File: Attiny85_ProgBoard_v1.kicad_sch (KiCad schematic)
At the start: 1 part, among them U1 ATtiny85V-10PU

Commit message: Designed PCB
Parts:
- added J1, J2, J3, J4, J5, J6, J7, J8: Conn_01x01_Female, Connector_Pin:PinHole_01x01, symbol Connector:Conn_01x01_Female
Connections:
- net at U1.1 (~{RESET}/PB5): now also J7.1 (Pin_1)
- net at U1.2 (XTAL1/PB3): now also J5.1 (Pin_1)
- net at U1.3 (XTAL2/PB4): now also J6.1 (Pin_1)
- net at U1.4 (GND): now also J8.1 (Pin_1)
- net at U1.5 (AREF/PB0): now also J2.1 (Pin_1)
- net at U1.6 (PB1): now also J3.1 (Pin_1)
- net at U1.7 (PB2): now also J4.1 (Pin_1)
- net at U1.8 (VCC): now also J1.1 (Pin_1)
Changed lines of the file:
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@@
 (kicad_sch (version 20230121) (generator eeschema)
   (paper "A4")
+  (wire (pts (xy 120.65 60.96) (xy 138.43 60.96))
+    (stroke (width 0) (type default))
+  )
+  (wire (pts (xy 135.89 71.12) (xy 151.13 71.12))
+    (stroke (width 0) (type default))
+  )
+  (wire (pts (xy 138.43 78.74) (xy 135.89 78.74))
+    (stroke (width 0) (type default))
+  )
+  (wire (pts (xy 135.89 88.9) (xy 152.4 88.9))
+    (stroke (width 0) (type default))
+  )
+  (wire (pts (xy 152.4 86.36) (xy 138.43 86.36))
+    (stroke (width 0) (type default))
+  )
+  (wire (pts (xy 135.89 76.2) (xy 140.97 76.2))
+    (stroke (width 0) (type default))
+  )
+  (wire (pts (xy 138.43 86.36) (xy 138.43 78.74))
+    (stroke (width 0) (type default))
+  )
+  (wire (pts (xy 135.89 73.66) (xy 151.13 73.66))
+    (stroke (width 0) (type default))
+  )
+  (wire (pts (xy 120.65 91.44) (xy 152.4 91.44))
+    (stroke (width 0) (type default))
+  )
+  (wire (pts (xy 140.97 83.82) (xy 152.4 83.82))
+    (stroke (width 0) (type default))
+  )
+  (wire (pts (xy 135.89 81.28) (xy 135.89 88.9))
+    (stroke (width 0) (type default))
+  )
+  (wire (pts (xy 138.43 66.04) (xy 138.43 60.96))
+    (stroke (width 0) (type default))
+  )
+  (wire (pts (xy 140.97 76.2) (xy 140.97 83.82))
+    (stroke (width 0) (type default))
+  )
+  (wire (pts (xy 151.13 66.04) (xy 138.43 66.04))
+    (stroke (width 0) (type default))
+  )
+  (wire (pts (xy 135.89 68.58) (xy 151.13 68.58))
+    (stroke (width 0) (type default))
+  )
   (symbol (lib_id "Attiny85_ProgBoard_v1-rescue:ATtiny85V-10PU-MCU_Microchip_ATtiny") (at 120.65 76.2 0) (unit 1)
     (in_bom yes) (on_board yes) (dnp no)
@@
         )
       )
+    )
+  )
+  (symbol (lib_id "Connector:Conn_01x01_Female") (at 157.48 88.9 0) (unit 1)
+    (in_bom yes) (on_board yes) (dnp no) (fields_autoplaced)
+    (property "Reference" "J7" (at 158.75 88.265 0)
+      (effects (font (size 1.27 1.27)) (justify left))
+    )
+    (property "Value" "Conn_01x01_Female" (at 158.75 90.805 0)
+      (effects (font (size 1.27 1.27)) (justify left))
+    )
+    (property "Footprint" "Connector_Pin:PinHole_01x01" (at 157.48 88.9 0)
+      (effects (font (size 1.27 1.27)) hide)
+    )
+    (property "Datasheet" "~" (at 157.48 88.9 0)
+      (effects (font (size 1.27 1.27)) hide)
+    )
+    (pin "1")
+    (instances
+      (project "Attiny85_ProgBoard_v1"
+        (path "/461172af-f3d0-444f-a1ea-3ea6bb3ec9d2"
+          (reference "J7") (unit 1)
+        )
+      )
+    )
+  )
+  (symbol (lib_id "Connector:Conn_01x01_Female") (at 156.21 73.66 0) (unit 1)
+    (in_bom yes) (on_board yes) (dnp no) (fields_autoplaced)
+    (property "Reference" "J4" (at 157.48 73.025 0)
+      (effects (font (size 1.27 1.27)) (justify left))
+    )
+    (property "Value" "Conn_01x01_Female" (at 157.48 75.565 0)
+      (effects (font (size 1.27 1.27)) (justify left))
+    )
+    (property "Footprint" "Connector_Pin:PinHole_01x01" (at 156.21 73.66 0)
+      (effects (font (size 1.27 1.27)) hide)
+    )
+    (property "Datasheet" "~" (at 156.21 73.66 0)
+      (effects (font (size 1.27 1.27)) hide)
+    )
+    (pin "1")
+    (instances
+      (project "Attiny85_ProgBoard_v1"
+        (path "/461172af-f3d0-444f-a1ea-3ea6bb3ec9d2"
+          (reference "J4") (unit 1)
+        )
+      )
+    )
+  )
+  (symbol (lib_id "Connector:Conn_01x01_Female") (at 156.21 66.04 0) (unit 1)
+    (in_bom yes) (on_board yes) (dnp no) (fields_autoplaced)
+    (property "Reference" "J1" (at 157.48 65.405 0)
+      (effects (font (size 1.27 1.27)) (justify left))
+    )
+    (property "Value" "Conn_01x01_Female" (at 157.48 67.945 0)
+      (effects (font (size 1.27 1.27)) (justify left))
+    )
+    (property "Footprint" "Connector_Pin:PinHole_01x01" (at 156.21 66.04 0)
+      (effects (font (size 1.27 1.27)) hide)
+    )
+    (property "Datasheet" "~" (at 156.21 66.04 0)
+      (effects (font (size 1.27 1.27)) hide)
+    )
+    (pin "1")
+    (instances
+      (project "Attiny85_ProgBoard_v1"
+        (path "/461172af-f3d0-444f-a1ea-3ea6bb3ec9d2"
+          (reference "J1") (unit 1)
+        )
+      )
+    )
+  )
+  (symbol (lib_id "Connector:Conn_01x01_Female") (at 157.48 83.82 0) (unit 1)
+    (in_bom yes) (on_board yes) (dnp no) (fields_autoplaced)
+    (property "Reference" "J5" (at 158.75 83.185 0)
+      (effects (font (size 1.27 1.27)) (justify left))
+    )
+    (property "Value" "Conn_01x01_Female" (at 158.75 85.725 0)
+      (effects (font (size 1.27 1.27)) (justify left))
+    )
+    (property "Footprint" "Connector_Pin:PinHole_01x01" (at 157.48 83.82 0)
+      (effects (font (size 1.27 1.27)) hide)
+    )
+    (property "Datasheet" "~" (at 157.48 83.82 0)
+      (effects (font (size 1.27 1.27)) hide)
+    )
+    (pin "1")
+    (instances
+      (project "Attiny85_ProgBoard_v1"
+        (path "/461172af-f3d0-444f-a1ea-3ea6bb3ec9d2"
+          (reference "J5") (unit 1)
+        )
+      )
+    )
+  )
+  (symbol (lib_id "Connector:Conn_01x01_Female") (at 157.48 86.36 0) (unit 1)
+    (in_bom yes) (on_board yes) (dnp no) (fields_autoplaced)
+    (property "Reference" "J6" (at 158.75 85.725 0)
+      (effects (font (size 1.27 1.27)) (justify left))
+    )
+    (property "Value" "Conn_01x01_Female" (at 158.75 88.265 0)
+      (effects (font (size 1.27 1.27)) (justify left))
+    )
+    (property "Footprint" "Connector_Pin:PinHole_01x01" (at 157.48 86.36 0)
+      (effects (font (size 1.27 1.27)) hide)
+    )
+    (property "Datasheet" "~" (at 157.48 86.36 0)
+      (effects (font (size 1.27 1.27)) hide)
+    )
+    (pin "1")
+    (instances
+      (project "Attiny85_ProgBoard_v1"
+        (path "/461172af-f3d0-444f-a1ea-3ea6bb3ec9d2"
+          (reference "J6") (unit 1)
+        )
+      )
+    )
+  )
+  (symbol (lib_id "Connector:Conn_01x01_Female") (at 157.48 91.44 0) (unit 1)
+    (in_bom yes) (on_board yes) (dnp no) (fields_autoplaced)
+    (property "Reference" "J8" (at 158.75 90.805 0)
+      (effects (font (size 1.27 1.27)) (justify left))
+    )
+    (property "Value" "Conn_01x01_Female" (at 158.75 93.345 0)
+      (effects (font (size 1.27 1.27)) (justify left))
+    )
+    (property "Footprint" "Connector_Pin:PinHole_01x01" (at 157.48 91.44 0)
+      (effects (font (size 1.27 1.27)) hide)
+    )
+    (property "Datasheet" "~" (at 157.48 91.44 0)
+      (effects (font (size 1.27 1.27)) hide)
+    )
+    (pin "1")
+    (instances
+      (project "Attiny85_ProgBoard_v1"
+        (path "/461172af-f3d0-444f-a1ea-3ea6bb3ec9d2"
+          (reference "J8") (unit 1)
+        )
+      )
+    )
+  )
+  (symbol (lib_id "Connector:Conn_01x01_Female") (at 156.21 68.58 0) (unit 1)
+    (in_bom yes) (on_board yes) (dnp no) (fields_autoplaced)
+    (property "Reference" "J2" (at 157.48 67.945 0)
+      (effects (font (size 1.27 1.27)) (justify left))
+    )
+    (property "Value" "Conn_01x01_Female" (at 157.48 70.485 0)
+      (effects (font (size 1.27 1.27)) (justify left))
+    )
+    (property "Footprint" "Connector_Pin:PinHole_01x01" (at 156.21 68.58 0)
+      (effects (font (size 1.27 1.27)) hide)
+    )
+    (property "Datasheet" "~" (at 156.21 68.58 0)
+      (effects (font (size 1.27 1.27)) hide)
+    )
+    (pin "1")
+    (instances
+      (project "Attiny85_ProgBoard_v1"
+        (path "/461172af-f3d0-444f-a1ea-3ea6bb3ec9d2"
+          (reference "J2") (unit 1)
+        )
+      )
+    )
+  )
+  (symbol (lib_id "Connector:Conn_01x01_Female") (at 156.21 71.12 0) (unit 1)
+    (in_bom yes) (on_board yes) (dnp no) (fields_autoplaced)
+    (property "Reference" "J3" (at 157.48 70.485 0)
+      (effects (font (size 1.27 1.27)) (justify left))
+    )
+    (property "Value" "Conn_01x01_Female" (at 157.48 73.025 0)
+      (effects (font (size 1.27 1.27)) (justify left))
+    )
+    (property "Footprint" "Connector_Pin:PinHole_01x01" (at 156.21 71.12 0)
+      (effects (font (size 1.27 1.27)) hide)
+    )
+    (property "Datasheet" "~" (at 156.21 71.12 0)
+      (effects (font (size 1.27 1.27)) hide)
+    )
+    (pin "1")
+    (instances
+      (project "Attiny85_ProgBoard_v1"
+        (path "/461172af-f3d0-444f-a1ea-3ea6bb3ec9d2"
+          (reference "J3") (unit 1)
+        )
+      )

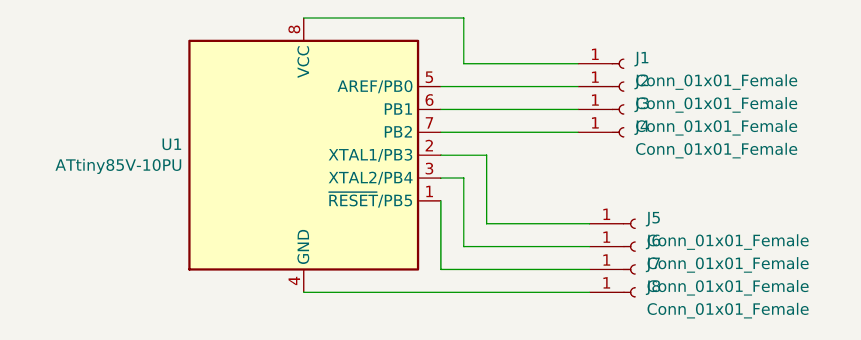
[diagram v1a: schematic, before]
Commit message: Added GND planes on top layer
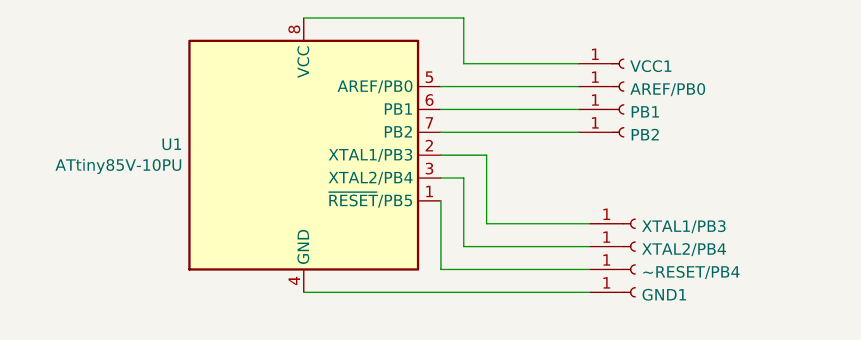
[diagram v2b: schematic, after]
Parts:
- renumbered J2 to AREF/PB0, J8 to GND1, J3 to PB1, J4 to PB2, J1 to VCC1, J5 to XTAL1/PB3, J6 to XTAL2/PB4, J7 to ~RESET/PB4
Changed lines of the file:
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@@
   (symbol (lib_id "Connector:Conn_01x01_Female") (at 157.48 88.9 0) (unit 1)
     (in_bom yes) (on_board yes) (dnp no) (fields_autoplaced)
-    (property "Reference" "J7" (at 158.75 88.265 0)
+    (property "Reference" "~RESET/PB4" (at 158.1912 89.2168 0)
       (effects (font (size 1.27 1.27)) (justify left))
     )
     (property "Value" "Conn_01x01_Female" (at 158.75 90.805 0)
-      (effects (font (size 1.27 1.27)) (justify left))
+      (effects (font (size 1.27 1.27)) (justify left) hide)
     )
     (property "Footprint" "Connector_Pin:PinHole_01x01" (at 157.48 88.9 0)
@@
       (project "Attiny85_ProgBoard_v1"
         (path "/461172af-f3d0-444f-a1ea-3ea6bb3ec9d2"
-          (reference "J7") (unit 1)
+          (reference "~RESET/PB4") (unit 1)
         )
       )
@@
   (symbol (lib_id "Connector:Conn_01x01_Female") (at 156.21 73.66 0) (unit 1)
     (in_bom yes) (on_board yes) (dnp no) (fields_autoplaced)
-    (property "Reference" "J4" (at 157.48 73.025 0)
+    (property "Reference" "PB2" (at 156.9212 73.9768 0)
       (effects (font (size 1.27 1.27)) (justify left))
     )
     (property "Value" "Conn_01x01_Female" (at 157.48 75.565 0)
-      (effects (font (size 1.27 1.27)) (justify left))
+      (effects (font (size 1.27 1.27)) (justify left) hide)
     )
     (property "Footprint" "Connector_Pin:PinHole_01x01" (at 156.21 73.66 0)
@@
       (project "Attiny85_ProgBoard_v1"
         (path "/461172af-f3d0-444f-a1ea-3ea6bb3ec9d2"
-          (reference "J4") (unit 1)
+          (reference "PB2") (unit 1)
         )
       )
@@
   (symbol (lib_id "Connector:Conn_01x01_Female") (at 156.21 66.04 0) (unit 1)
     (in_bom yes) (on_board yes) (dnp no) (fields_autoplaced)
-    (property "Reference" "J1" (at 157.48 65.405 0)
+    (property "Reference" "VCC1" (at 156.9212 66.3568 0)
       (effects (font (size 1.27 1.27)) (justify left))
     )
-    (property "Value" "Conn_01x01_Female" (at 157.48 67.945 0)
-      (effects (font (size 1.27 1.27)) (justify left))
+    (property "Value" "Conn_01x01_Female" (at 156.9212 67.3173 0)
+      (effects (font (size 1.27 1.27)) (justify left) hide)
     )
     (property "Footprint" "Connector_Pin:PinHole_01x01" (at 156.21 66.04 0)
@@
       (project "Attiny85_ProgBoard_v1"
         (path "/461172af-f3d0-444f-a1ea-3ea6bb3ec9d2"
-          (reference "J1") (unit 1)
+          (reference "VCC1") (unit 1)
         )
       )
@@
   (symbol (lib_id "Connector:Conn_01x01_Female") (at 157.48 83.82 0) (unit 1)
     (in_bom yes) (on_board yes) (dnp no) (fields_autoplaced)
-    (property "Reference" "J5" (at 158.75 83.185 0)
+    (property "Reference" "XTAL1/PB3" (at 158.1912 84.1368 0)
       (effects (font (size 1.27 1.27)) (justify left))
     )
     (property "Value" "Conn_01x01_Female" (at 158.75 85.725 0)
-      (effects (font (size 1.27 1.27)) (justify left))
+      (effects (font (size 1.27 1.27)) (justify left) hide)
     )
     (property "Footprint" "Connector_Pin:PinHole_01x01" (at 157.48 83.82 0)
@@
       (project "Attiny85_ProgBoard_v1"
         (path "/461172af-f3d0-444f-a1ea-3ea6bb3ec9d2"
-          (reference "J5") (unit 1)
+          (reference "XTAL1/PB3") (unit 1)
         )
       )
@@
   (symbol (lib_id "Connector:Conn_01x01_Female") (at 157.48 86.36 0) (unit 1)
     (in_bom yes) (on_board yes) (dnp no) (fields_autoplaced)
-    (property "Reference" "J6" (at 158.75 85.725 0)
+    (property "Reference" "XTAL2/PB4" (at 158.1912 86.6768 0)
       (effects (font (size 1.27 1.27)) (justify left))
     )
     (property "Value" "Conn_01x01_Female" (at 158.75 88.265 0)
-      (effects (font (size 1.27 1.27)) (justify left))
+      (effects (font (size 1.27 1.27)) (justify left) hide)
     )
     (property "Footprint" "Connector_Pin:PinHole_01x01" (at 157.48 86.36 0)
@@
       (project "Attiny85_ProgBoard_v1"
         (path "/461172af-f3d0-444f-a1ea-3ea6bb3ec9d2"
-          (reference "J6") (unit 1)
+          (reference "XTAL2/PB4") (unit 1)
         )
       )
@@
   (symbol (lib_id "Connector:Conn_01x01_Female") (at 157.48 91.44 0) (unit 1)
     (in_bom yes) (on_board yes) (dnp no) (fields_autoplaced)
-    (property "Reference" "J8" (at 158.75 90.805 0)
+    (property "Reference" "GND1" (at 158.1912 91.7568 0)
       (effects (font (size 1.27 1.27)) (justify left))
     )
     (property "Value" "Conn_01x01_Female" (at 158.75 93.345 0)
-      (effects (font (size 1.27 1.27)) (justify left))
+      (effects (font (size 1.27 1.27)) (justify left) hide)
     )
     (property "Footprint" "Connector_Pin:PinHole_01x01" (at 157.48 91.44 0)
@@
       (project "Attiny85_ProgBoard_v1"
         (path "/461172af-f3d0-444f-a1ea-3ea6bb3ec9d2"
-          (reference "J8") (unit 1)
+          (reference "GND1") (unit 1)
         )
       )
@@
   (symbol (lib_id "Connector:Conn_01x01_Female") (at 156.21 68.58 0) (unit 1)
     (in_bom yes) (on_board yes) (dnp no) (fields_autoplaced)
-    (property "Reference" "J2" (at 157.48 67.945 0)
+    (property "Reference" "AREF/PB0" (at 156.9212 68.8968 0)
       (effects (font (size 1.27 1.27)) (justify left))
     )
     (property "Value" "Conn_01x01_Female" (at 157.48 70.485 0)
-      (effects (font (size 1.27 1.27)) (justify left))
+      (effects (font (size 1.27 1.27)) (justify left) hide)
     )
     (property "Footprint" "Connector_Pin:PinHole_01x01" (at 156.21 68.58 0)
@@
       (project "Attiny85_ProgBoard_v1"
         (path "/461172af-f3d0-444f-a1ea-3ea6bb3ec9d2"
-          (reference "J2") (unit 1)
+          (reference "AREF/PB0") (unit 1)
         )
       )
@@
   (symbol (lib_id "Connector:Conn_01x01_Female") (at 156.21 71.12 0) (unit 1)
     (in_bom yes) (on_board yes) (dnp no) (fields_autoplaced)
-    (property "Reference" "J3" (at 157.48 70.485 0)
+    (property "Reference" "PB1" (at 156.9212 71.4368 0)
       (effects (font (size 1.27 1.27)) (justify left))
     )
     (property "Value" "Conn_01x01_Female" (at 157.48 73.025 0)
-      (effects (font (size 1.27 1.27)) (justify left))
+      (effects (font (size 1.27 1.27)) (justify left) hide)
     )
     (property "Footprint" "Connector_Pin:PinHole_01x01" (at 156.21 71.12 0)
@@
       (project "Attiny85_ProgBoard_v1"
         (path "/461172af-f3d0-444f-a1ea-3ea6bb3ec9d2"
-          (reference "J3") (unit 1)
+          (reference "PB1") (unit 1)
         )
       )

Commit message: Added dedicated library
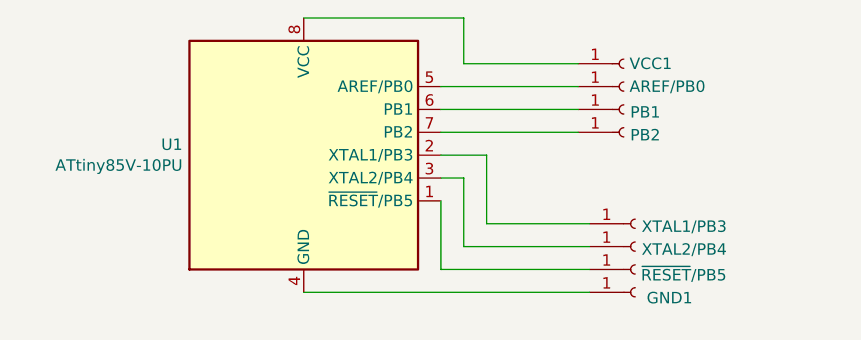
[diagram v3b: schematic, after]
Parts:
- AREF/PB0, GND1, PB1, PB2, VCC1, XTAL1/PB3, XTAL2/PB4: footprint Connector_Pin:PinHole_01x01 -> PinHole:PinHole_01x01
- ~{RESET}/PB5: renamed from ~RESET/PB4; footprint Connector_Pin:PinHole_01x01 -> PinHole:PinHole_01x01
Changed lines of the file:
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@@
   )
   (symbol (lib_id "Connector:Conn_01x01_Female") (at 157.48 88.9 0) (unit 1)
-    (in_bom yes) (on_board yes) (dnp no) (fields_autoplaced)
-    (property "Reference" "~RESET/PB4" (at 158.1912 89.2168 0)
+    (in_bom yes) (on_board yes) (dnp no)
+    (property "Reference" "~{RESET}/PB5" (at 158.115 89.535 0)
       (effects (font (size 1.27 1.27)) (justify left))
     )
@@
       (effects (font (size 1.27 1.27)) (justify left) hide)
     )
-    (property "Footprint" "Connector_Pin:PinHole_01x01" (at 157.48 88.9 0)
+    (property "Footprint" "PinHole:PinHole_01x01" (at 157.48 88.9 0)
       (effects (font (size 1.27 1.27)) hide)
     )
@@
       (project "Attiny85_ProgBoard_v1"
         (path "/461172af-f3d0-444f-a1ea-3ea6bb3ec9d2"
-          (reference "~RESET/PB4") (unit 1)
+          (reference "~{RESET}/PB5") (unit 1)
         )
       )
@@
       (effects (font (size 1.27 1.27)) (justify left) hide)
     )
-    (property "Footprint" "Connector_Pin:PinHole_01x01" (at 156.21 73.66 0)
+    (property "Footprint" "PinHole:PinHole_01x01" (at 156.21 73.66 0)
       (effects (font (size 1.27 1.27)) hide)
     )
@@
   )
   (symbol (lib_id "Connector:Conn_01x01_Female") (at 156.21 66.04 0) (unit 1)
-    (in_bom yes) (on_board yes) (dnp no) (fields_autoplaced)
-    (property "Reference" "VCC1" (at 156.9212 66.3568 0)
+    (in_bom yes) (on_board yes) (dnp no)
+    (property "Reference" "VCC1" (at 156.845 66.04 0)
       (effects (font (size 1.27 1.27)) (justify left))
     )
@@
       (effects (font (size 1.27 1.27)) (justify left) hide)
     )
-    (property "Footprint" "Connector_Pin:PinHole_01x01" (at 156.21 66.04 0)
+    (property "Footprint" "PinHole:PinHole_01x01" (at 156.21 66.04 0)
       (effects (font (size 1.27 1.27)) hide)
     )
@@
       (effects (font (size 1.27 1.27)) (justify left) hide)
     )
-    (property "Footprint" "Connector_Pin:PinHole_01x01" (at 157.48 83.82 0)
+    (property "Footprint" "PinHole:PinHole_01x01" (at 157.48 83.82 0)
       (effects (font (size 1.27 1.27)) hide)
     )
@@
   )
   (symbol (lib_id "Connector:Conn_01x01_Female") (at 157.48 86.36 0) (unit 1)
-    (in_bom yes) (on_board yes) (dnp no) (fields_autoplaced)
+    (in_bom yes) (on_board yes) (dnp no)
     (property "Reference" "XTAL2/PB4" (at 158.1912 86.6768 0)
       (effects (font (size 1.27 1.27)) (justify left))
@@
       (effects (font (size 1.27 1.27)) (justify left) hide)
     )
-    (property "Footprint" "Connector_Pin:PinHole_01x01" (at 157.48 86.36 0)
+    (property "Footprint" "PinHole:PinHole_01x01" (at 157.48 86.36 0)
       (effects (font (size 1.27 1.27)) hide)
     )
@@
   (symbol (lib_id "Connector:Conn_01x01_Female") (at 157.48 91.44 0) (unit 1)
     (in_bom yes) (on_board yes) (dnp no) (fields_autoplaced)
-    (property "Reference" "GND1" (at 158.1912 91.7568 0)
+    (property "Reference" "GND1" (at 158.75 92.075 0)
       (effects (font (size 1.27 1.27)) (justify left))
     )
@@
       (effects (font (size 1.27 1.27)) (justify left) hide)
     )
-    (property "Footprint" "Connector_Pin:PinHole_01x01" (at 157.48 91.44 0)
+    (property "Footprint" "PinHole:PinHole_01x01" (at 157.48 91.44 0)
       (effects (font (size 1.27 1.27)) hide)
     )
@@
   )
   (symbol (lib_id "Connector:Conn_01x01_Female") (at 156.21 68.58 0) (unit 1)
-    (in_bom yes) (on_board yes) (dnp no) (fields_autoplaced)
-    (property "Reference" "AREF/PB0" (at 156.9212 68.8968 0)
+    (in_bom yes) (on_board yes) (dnp no)
+    (property "Reference" "AREF/PB0" (at 156.845 68.58 0)
       (effects (font (size 1.27 1.27)) (justify left))
     )
@@
       (effects (font (size 1.27 1.27)) (justify left) hide)
     )
-    (property "Footprint" "Connector_Pin:PinHole_01x01" (at 156.21 68.58 0)
+    (property "Footprint" "PinHole:PinHole_01x01" (at 156.21 68.58 0)
       (effects (font (size 1.27 1.27)) hide)
     )
@@
       (effects (font (size 1.27 1.27)) (justify left) hide)
     )
-    (property "Footprint" "Connector_Pin:PinHole_01x01" (at 156.21 71.12 0)
+    (property "Footprint" "PinHole:PinHole_01x01" (at 156.21 71.12 0)
       (effects (font (size 1.27 1.27)) hide)
     )
